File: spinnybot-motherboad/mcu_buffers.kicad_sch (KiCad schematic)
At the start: 12 parts, among them Q3 BC846, U2 XBP9B-DMWTB002, U5 ESP32-DEVKITC-32D, U6 SN74AHCT541DW, U7 SN74AHCT541DW

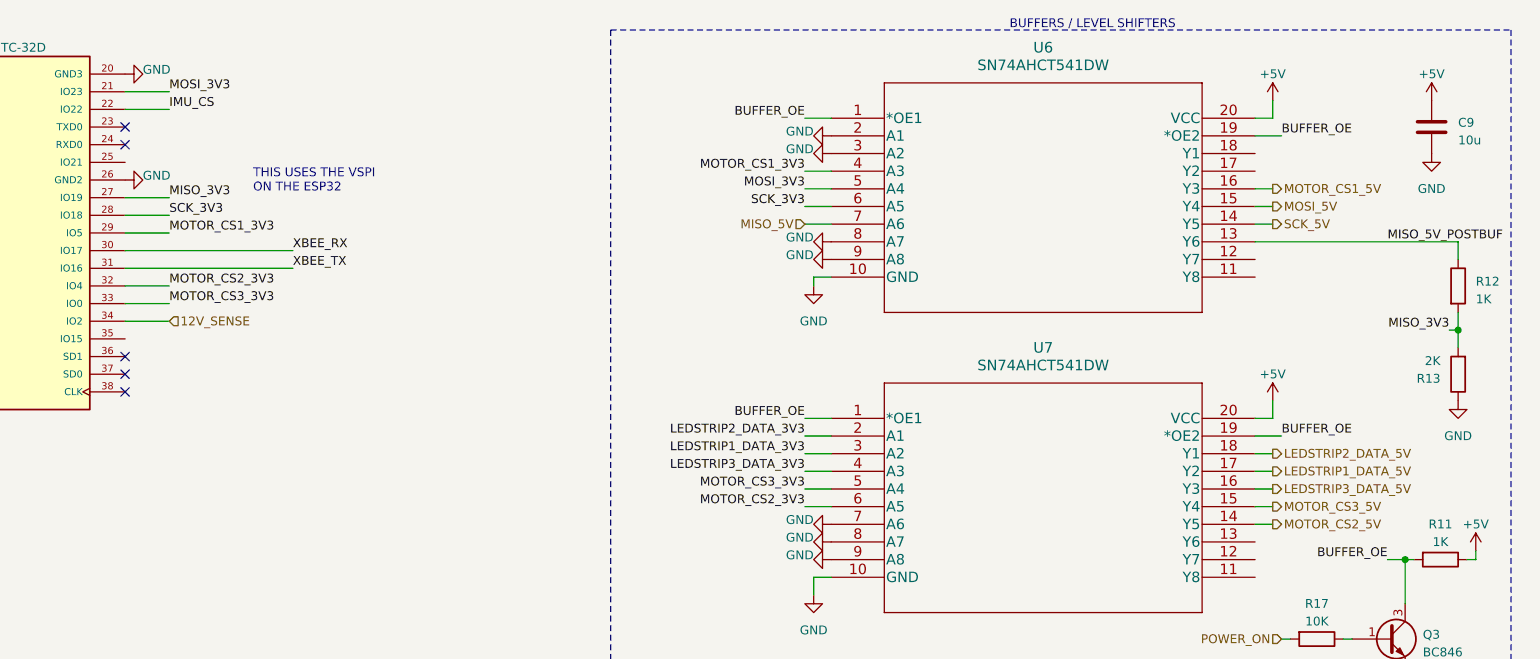
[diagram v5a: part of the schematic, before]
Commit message: removed some old signals
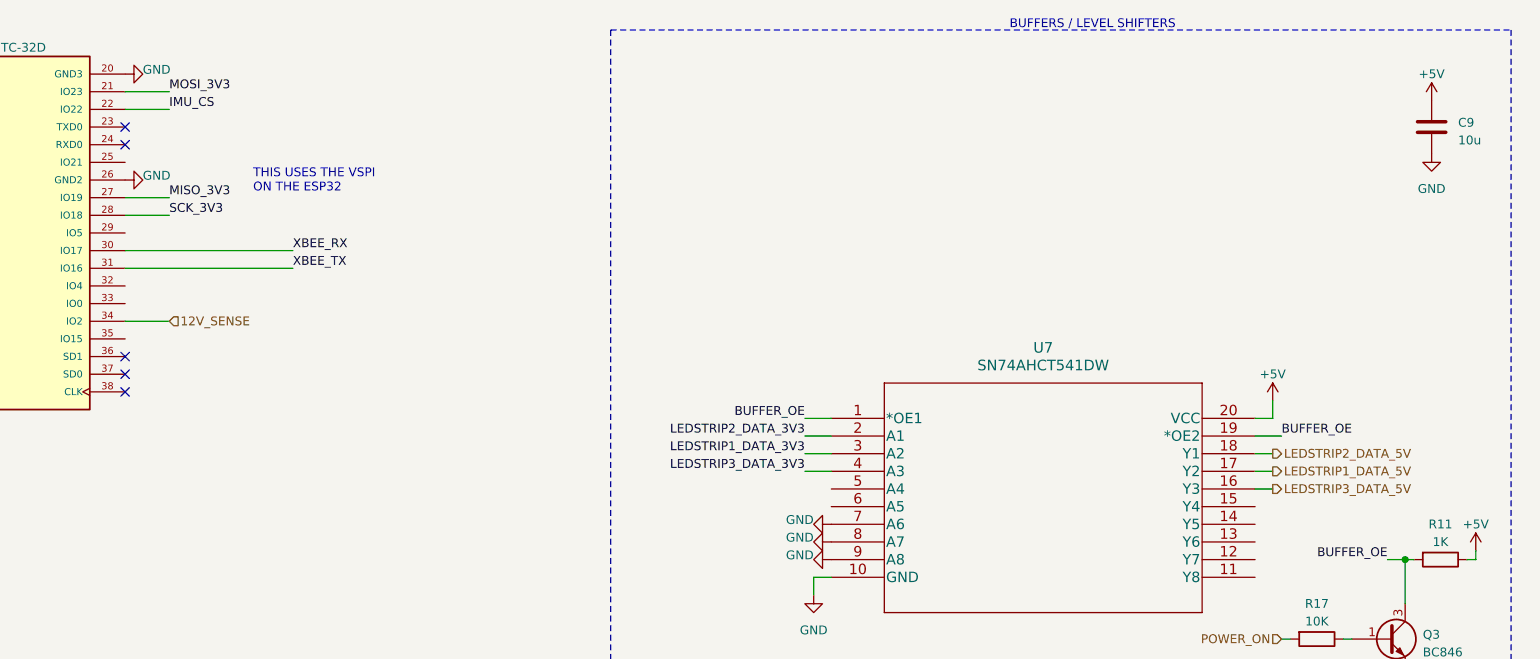
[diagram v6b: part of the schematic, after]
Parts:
- removed R12: 1K, Resistor_SMD:R_0805_2012Metric_Pad1.20x1.40mm_HandSolder, symbol Device:R
- removed R13: 2K, Resistor_SMD:R_0805_2012Metric_Pad1.20x1.40mm_HandSolder, symbol Device:R
- removed U6: SN74AHCT541DW, SN74AHCT541DW:SN74AHCT541DW, symbol SN74AHCT541DW:SN74AHCT541DW
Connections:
- net MOTOR_CS1_3V3: no longer names the net of U5.29 (IO5)
- net MOTOR_CS2_3V3: no longer names the net of U5.32 (IO4)
- net MOTOR_CS2_3V3: no longer U7.6 (A5)
- net MOTOR_CS2_5V: no longer names the net of U7.14 (Y5)
- net MOTOR_CS3_3V3: no longer names the net of U5.33 (IO0)
- net MOTOR_CS3_3V3: no longer U7.5 (A4)
- net MOTOR_CS3_5V: no longer names the net of U7.15 (Y4)

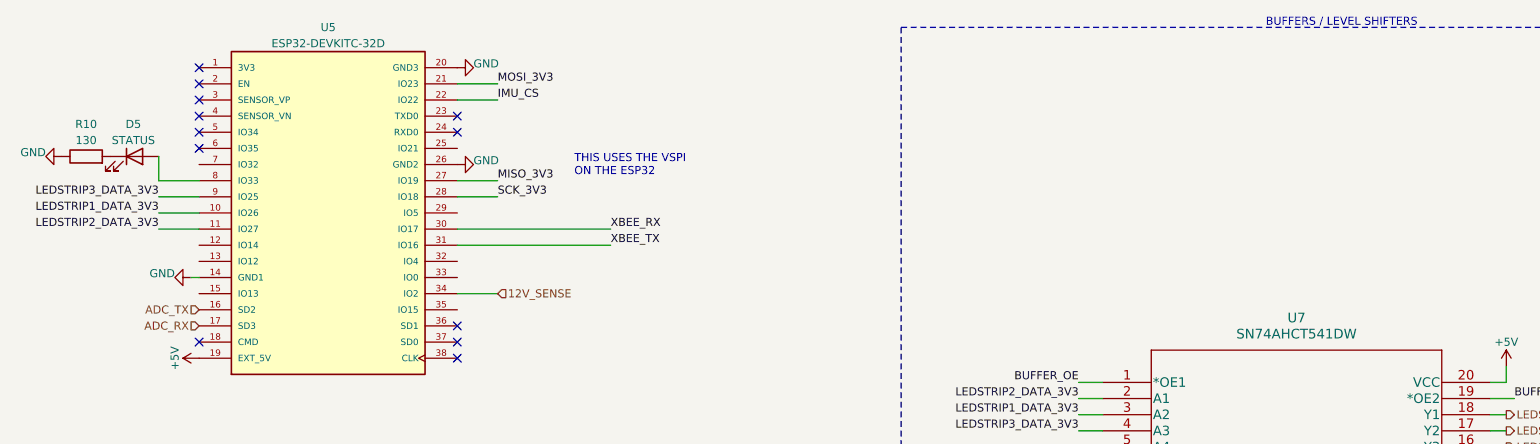
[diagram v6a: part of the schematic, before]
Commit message: Made ESP32 connections, added logic level shifter
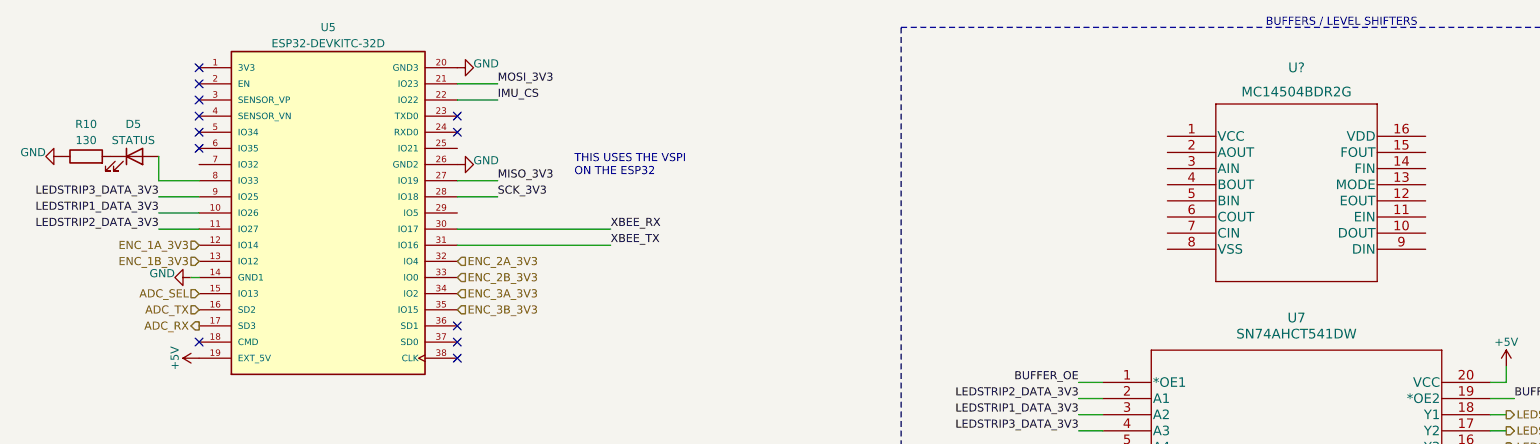
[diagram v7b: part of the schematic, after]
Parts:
- added U?: MC14504BDR2G, SOIC-16_ONS, symbol MC14504BDR2G:MC14504BDR2G
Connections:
- net ENC_1A_3V3: now reaches U5.12 (IO14)
- net ENC_1B_3V3: now reaches U5.13 (IO12)
- net ADC_SEL: now reaches U5.15 (IO13)
- net ENC_2A_3V3: now reaches U5.32 (IO4)
- net ENC_2B_3V3: now reaches U5.33 (IO0)
- net ENC_3B_3V3: now reaches U5.35 (IO15)
- net 12V_SENSE renamed ENC_3A_3V3
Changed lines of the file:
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@@
   (no_connect (at 82.55 31.75))
   (no_connect (at 82.55 34.29))
-  (wire (pts (xy 82.55 59.69) (xy 88.9 59.69))
-    (stroke (width 0) (type solid) (color 0 0 0 0))
-  )
   (wire (pts (xy 106.68 49.53) (xy 82.55 49.53))
     (stroke (width 0) (type solid) (color 0 0 0 0))
@@
     (effects (font (size 1.27 1.27)) (justify left bottom))
   )
+  (hierarchical_label "ENC_1B_3V3" (shape input) (at 41.91 54.61 180)
+    (effects (font (size 1.27 1.27)) (justify right))
+  )
+  (hierarchical_label "ENC_2B_3V3" (shape input) (at 82.55 57.15 0)
+    (effects (font (size 1.27 1.27)) (justify left))
+  )
   (hierarchical_label "LEDSTRIP2_DATA_5V" (shape output) (at 247.65 78.74 0)
     (effects (font (size 1.27 1.27)) (justify left))
   )
+  (hierarchical_label "ENC_3A_3V3" (shape input) (at 82.55 59.69 0)
+    (effects (font (size 1.27 1.27)) (justify left))
+  )
   (hierarchical_label "POWER_ON" (shape input) (at 248.92 105.41 180)
     (effects (font (size 1.27 1.27)) (justify right))
@@
     (effects (font (size 1.27 1.27)) (justify left))
   )
+  (hierarchical_label "ENC_2A_3V3" (shape input) (at 82.55 54.61 0)
+    (effects (font (size 1.27 1.27)) (justify left))
+  )
   (hierarchical_label "ADC_TX" (shape input) (at 41.91 62.23 180)
     (effects (font (size 1.27 1.27)) (justify right))
   )
-  (hierarchical_label "12V_SENSE" (shape input) (at 88.9 59.69 0)
+  (hierarchical_label "ENC_1A_3V3" (shape input) (at 41.91 52.07 180)
+    (effects (font (size 1.27 1.27)) (justify right))
+  )
+  (hierarchical_label "ADC_SEL" (shape input) (at 41.91 59.69 180)
+    (effects (font (size 1.27 1.27)) (justify right))
+  )
+  (hierarchical_label "ENC_3B_3V3" (shape input) (at 82.55 62.23 0)
     (effects (font (size 1.27 1.27)) (justify left))
   )
@@
     (effects (font (size 1.27 1.27)) (justify left))
   )
-  (hierarchical_label "ADC_RX" (shape input) (at 41.91 64.77 180)
+  (hierarchical_label "ADC_RX" (shape output) (at 41.91 64.77 180)
     (effects (font (size 1.27 1.27)) (justify right))
   )
@@
     (pin "1")
   )
+  (symbol (lib_id "MC14504BDR2G:MC14504BDR2G") (at 194.31 34.925 0) (unit 1)
+    (in_bom yes) (on_board yes) (fields_autoplaced)
+    (property "Reference" "U?" (id 0) (at 214.63 24.13 0)
+      (effects (font (size 1.524 1.524)))
+    )
+    (property "Value" "MC14504BDR2G" (id 1) (at 214.63 27.94 0)
+      (effects (font (size 1.524 1.524)))
+    )
+    (property "Footprint" "SOIC-16_ONS" (id 2) (at 214.63 28.829 0)
+      (effects (font (size 1.524 1.524)) hide)
+    )
+    (property "Datasheet" "" (id 3) (at 194.31 34.925 0)
+      (effects (font (size 1.524 1.524)))
+    )
+    (pin "1")
+    (pin "10")
+    (pin "11")
+    (pin "12")
+    (pin "13")
+    (pin "14")
+    (pin "15")
+    (pin "16")
+    (pin "2")
+    (pin "3")
+    (pin "4")
+    (pin "5")
+    (pin "6")
+    (pin "7")
+    (pin "8")
+    (pin "9")
+  )
   (symbol (lib_id "Device:LED") (at 31.75 38.1 0) (unit 1)

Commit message: PCB schematic (hopefully) finished
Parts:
- removed D5: STATUS, LED_SMD:LED_0805_2012Metric_Pad1.15x1.40mm_HandSolder, symbol Device:LED
- removed R10: 130, Resistor_SMD:R_0805_2012Metric_Pad1.20x1.40mm_HandSolder, symbol Device:R
- added C?: 10u, Capacitor_SMD:C_1206_3216Metric_Pad1.33x1.80mm_HandSolder, symbol Device:C
- added D?: STATUS, LED_SMD:LED_0805_2012Metric_Pad1.15x1.40mm_HandSolder, symbol Device:LED
- added JP?: SolderJumper_2_Bridged, symbol Jumper:SolderJumper_2_Bridged
- added JP?: SolderJumper_2_Open, symbol Jumper:SolderJumper_2_Open
- added R?: 130, Resistor_SMD:R_0805_2012Metric_Pad1.20x1.40mm_HandSolder, symbol Device:R
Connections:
- net +3V3: now also U?.16 (VDD), C?.1
- net +5V: now also U?.1 (VCC), JP?.2 (B)
- net ENC_1A_3V3: now also U?.2 (AOUT)
- net ENC_1B_3V3: now also U?.4 (BOUT)
- net ENC_2A_3V3: now also U?.6 (COUT)
- net ENC_2B_3V3: now also U?.10 (DOUT)
- net ENC_3A_3V3: now also U?.12 (EOUT)
- net ENC_3B_3V3: now also U?.15 (FOUT)
- net GND: now also U?.8 (VSS), C?.2, JP?.1 (A), R?.1
- net LEDSTRIP3_DATA_3V3: now also U5.25 (IO21); no longer U5.9 (IO25)
- net ENC_3A_5V: now reaches U?.11 (EIN)
- net at U?.13 (MODE): now also JP?.1 (A), JP?.2 (B)
- net ENC_3B_5V: now reaches U?.14 (FIN)
- net ENC_1A_5V: now reaches U?.3 (AIN)
- net ENC_1B_5V: now reaches U?.5 (BIN)
- net ENC_2A_5V: now reaches U?.7 (CIN)
- net ENC_2B_5V: now reaches U?.9 (DIN)
- net ESC_S2: now reaches U5.8 (IO33)
- net at U5.29 (IO5): now also D?.2 (A)
- net ESC_S1: now reaches U5.7 (IO32)
- new net: D?.1 (K), R?.2
- new net ESS_S3: U5.9 (IO25)
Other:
- moved on the sheet: C9, U5, U?
